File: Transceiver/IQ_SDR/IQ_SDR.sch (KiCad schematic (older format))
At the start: 198 parts, among them CON1 SJ1-3523N, J1 ANT, J10 LO_I, J11 LO_Q, J12 GNDA, J13 I_IN, J14 Q_IN, J15 +5V, J16 4.3V, J17 I_OUT, J18 Q_OUT, J19 Conn_01x01_Male, J2 GND, J20 Conn_01x01_Male, J21 V_CC, J22 Ba, J23 Bb, J24 Cb, J25 Ca, J26 Gb, J27 Ga, J28 Conn_01x02_Female, J29 Conn_01x02_Female, J3 V_IN pin header, J30 Conn_01x02_Female, J31 Conn_01x02_Female, J32 Conn_01x02_Female, J33 Conn_01x02_Female, J34 Conn_01x04_Male, J4 GND, J5 V_IN, J6 FIL_O, J7 CLK1, J8 CLK2, J9 CLK0, P1 BNC, P2 SMA, P3 SMA, P4 SMA, Q1 MMBT2222A-TP, Q10 MMBT2222A-TP, Q11 MMBT2222A-TP, Q2 2N3904, Q3 2N3904, Q4 2N3904, Q5 2N3904, Q6 MMBT2222A-TP, Q7 MMBT2222A-TP, Q8 IRF510PBF, Q9 IRF510PBF, T1 Transformer_1P_SS, T2 Transformer_1P_1S, T3 Transformer_1P_1S, T4 Transformer_SP_1S, T5 BN43-6802, U1 FST3253 or TS3A5017, U2 Si5351A-B-GT, U3 TS5A23157, U4 LM4562 or LT6231, U5 74ALVC74D, U6 Blue Pill, Y1 CX3225

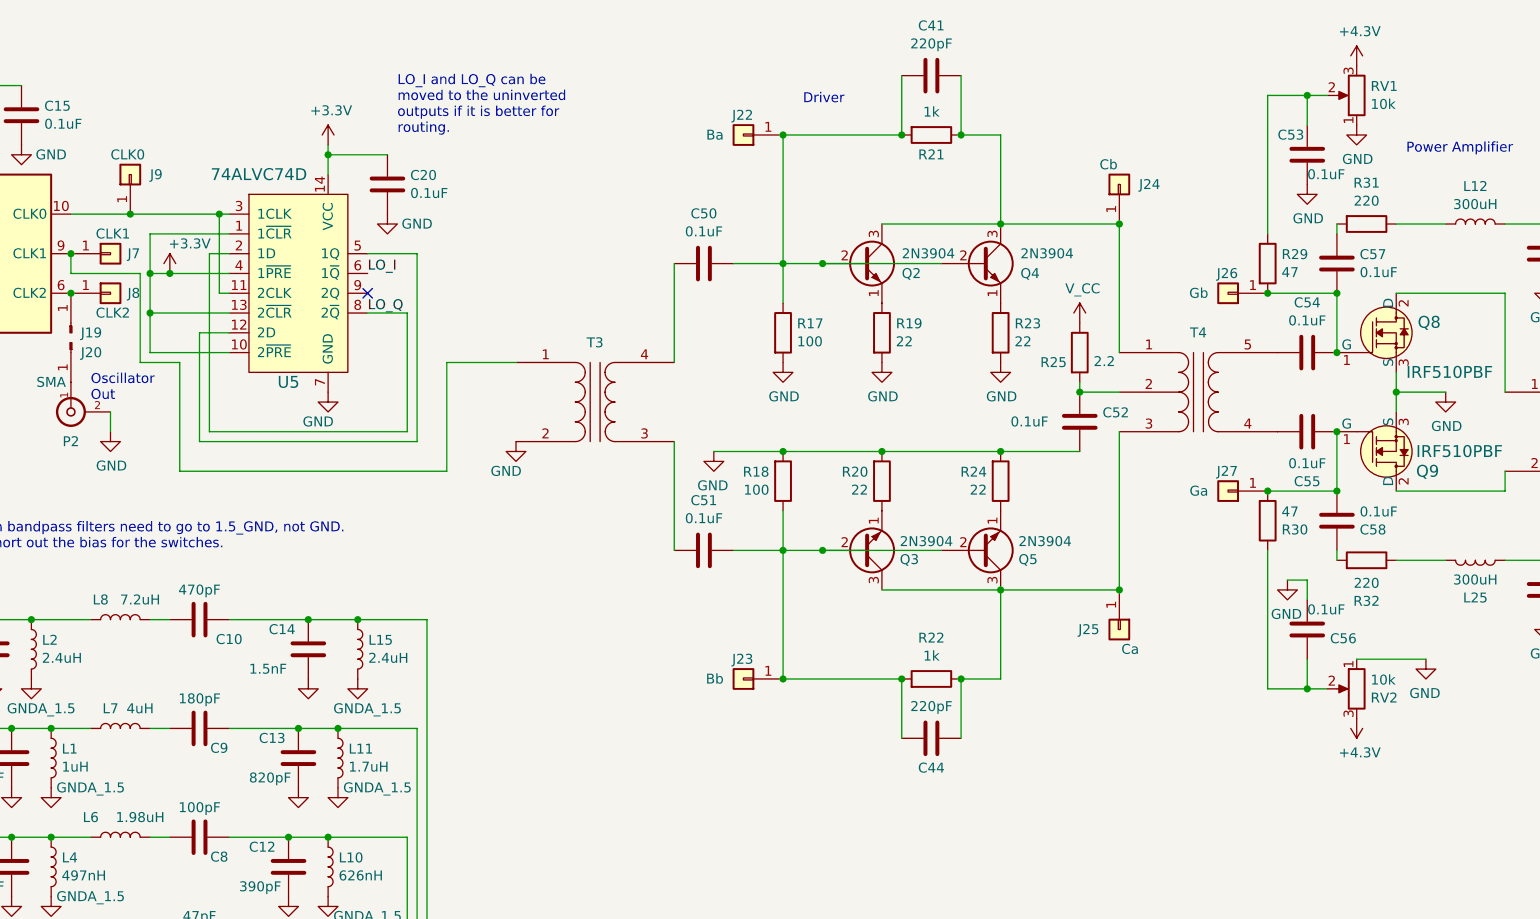
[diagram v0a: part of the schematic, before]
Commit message: Further change to schematic and moving simulations
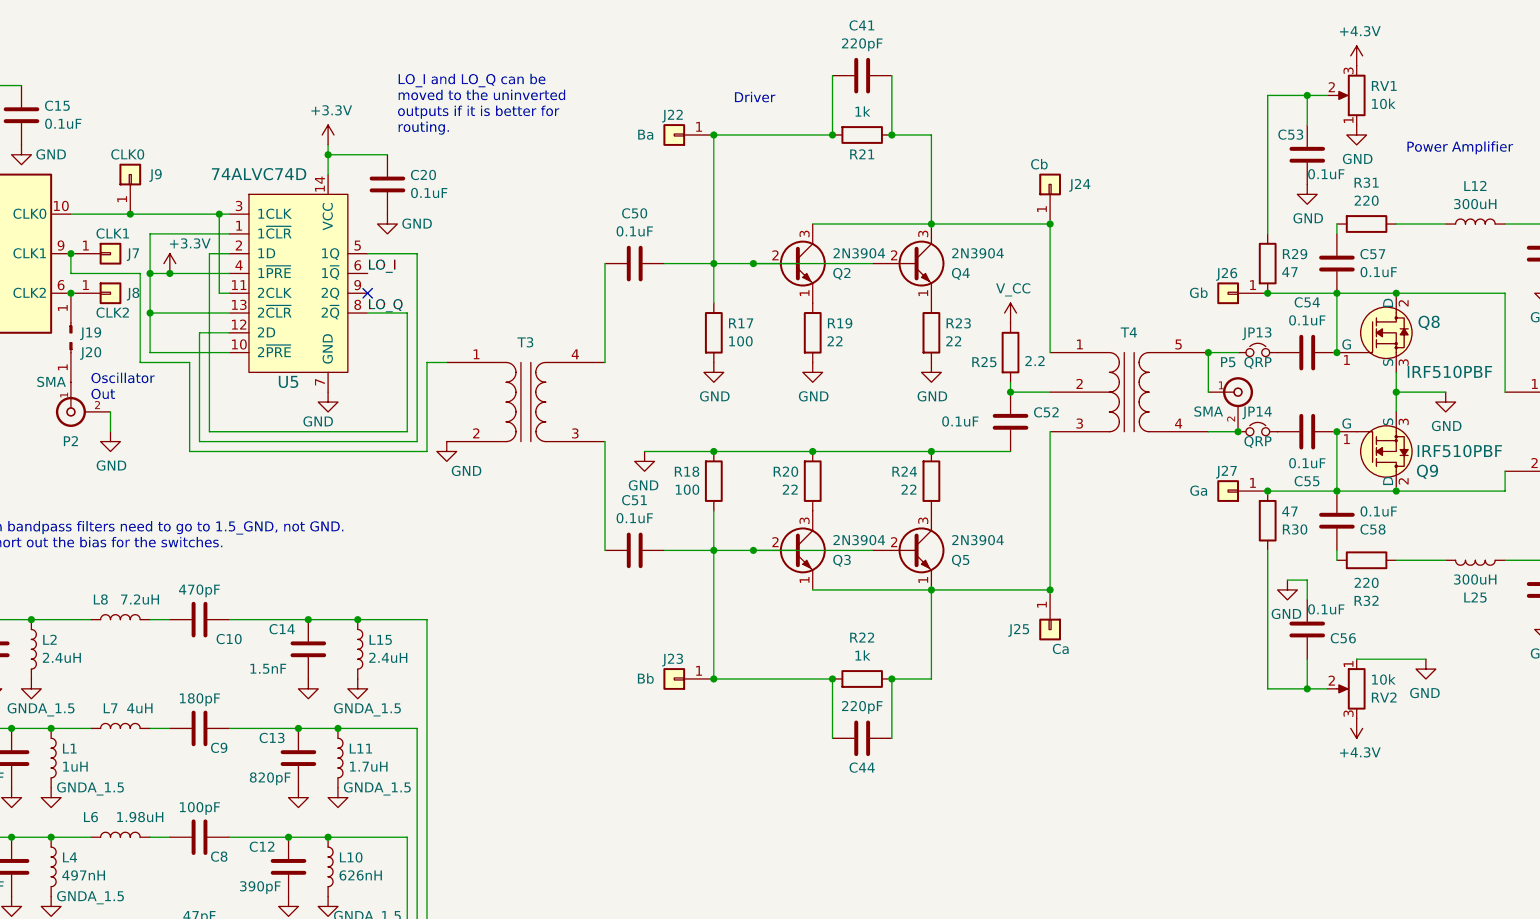
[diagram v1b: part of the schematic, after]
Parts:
- added JP13, JP14: QRP, Pin_Headers:Pin_Header_Straight_1x02_Pitch2.54mm, symbol Device:Jumper_NC_Small
- added P5: SMA, SMA:SMA_EDGE, symbol IQ_SDR-rescue:BNC-lt6231
- Q2, Q3, Q4, Q5: footprint Package_TO_SOT_THT:TO-92_Inline -> digikey-footprints:TO-92-3
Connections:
- net at C54.1, C57.1, J26.1 (Pin_1)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: now also Q8.2 (D), T5.1 (AA)
- net at C54.2: now also JP13.2; no longer T4.5 (S2)
- net at C55.1, C58.1, J27.1 (Pin_1)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: now also Q9.2 (D), T5.2 (AB)
- net at T4.4 (S1): now also JP14.1, P5.2 (Ext); no longer C55.2
- net at Q3.1 (E): now also C44.1, J25.1 (Pin_1), Q5.1 (E), R22.1, T4.3 (PR2); no longer R20.1
- net at R24.1: now also Q5.3 (C); no longer Q5.1 (E)
- new net: JP13.1, P5.1 (In), T4.5 (S2)
- new net: C55.2, JP14.2
- new net: Q3.3 (C), R20.1
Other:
- moved on the sheet: C41, C44, C50, C51, C52, J22, J23, J24, J25, Q2, R17, R18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

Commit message: PCB initial design
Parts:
- J34: footprint Pin_Headers:Pin_Header_Angled_1x04_Pitch2.54mm -> Pin_Headers:Pin_Header_Straight_1x04_Pitch2.54mm
- JP4: footprint Pin_Headers:Pin_Header_Straight_1x02_Pitch2.00mm_SMD_Pin1Right -> Pin_Headers:Pin_Header_Straight_1x02_Pitch2.54mm
- R26, R27: footprint Resistors_SMD:R_0805 -> Socket_Strips:Socket_Strip_Straight_1x02_Pitch2.54mm
- T1, T4: footprint IQ_SDR:Transformer_Toroid_Tapped_Secondary_Horizontal_D14.0mm_Amidon-T50 -> IQ_SDR:T50-2_vertical_5_pin
- T2, T3: footprint IQ_SDR:Transformer_Toroid_Tapped_Secondary_Horizontal_D14.0mm_Amidon-T50 -> IQ_SDR:T50-2_vertical_4_pin
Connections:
- net ANT_RLY: now also A1.26 (A7)
- net GND: now also T3.1 (AA); no longer T3.2 (AB)
- net SCL: now also R16.1, U6.PB6; no longer R15.1
- net SDA: now also R15.1, U6.PB7; no longer R16.1
- net TX_BAND: now also A1.25 (A6)
- net at J7.1 (Pin_1), U2.9 (CLK1): now also T3.2 (AB); no longer T3.1 (AA)
- net RFm: now reaches P1.1 (In), RLY2.9 (COM2)
- net RFb: now reaches P1.2 (Ext), RLY2.4 (COM1)
- net at C54.1, C57.1, J26.1 (Pin_1)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: no longer Q8.2 (D), T5.1 (AA)
- net PA_V_CCb: now reaches L12.1, R31.1
- net PA_V_CCb: now also Q8.2 (D), T5.1 (AA)
- net RFh: now reaches C46.1, JP12.2, L21.2, RLY1.10 (NC2)
- net RFg: now reaches C38.1, JP12.1, L17.1, RLY1.3 (NC1)
- net RFd: now reaches C47.1, L22.2, RLY1.4 (COM1)
- net RFc: now reaches C35.2, RLY1.9 (COM2)
- net at JP13.1, P5.1 (In): now also T4.4 (S1); no longer T4.5 (S2)
- net at JP14.1, P5.2 (Ext): now also T4.5 (S2); no longer T4.4 (S1)
- net at C55.1, C58.1, J27.1 (Pin_1)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: no longer Q9.2 (D), T5.2 (AB)
- net PA_V_CCc: now reaches L25.1, R32.1
- net PA_V_CCc: now also Q9.2 (D), T5.2 (AB)
- net Rfe: now reaches C34.1, JP11.1, L14.1, P4.1 (In)
- net RFf: now reaches C39.1, L14.2, L18.1
- net RFj: now reaches C43.1, L18.2, L22.1
- net RFk: now reaches C42.1, L17.2, L21.1
- net RFa: now reaches P4.2 (Ext), RLY2.5 (NO1), T5.3 (SA)
- net at C41.1, J24.1 (Pin_1), Q2.3 (C)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: now also T4.3 (PR2); no longer T4.1 (PR1)
- net at C50.2: now also T3.3 (SA); no longer T3.4 (SB)
- net at C44.1, J25.1 (Pin_1), R22.1: now also Q3.3 (C), Q5.3 (C), T4.1 (PR1); no longer Q3.1 (E), Q5.1 (E), T4.3 (PR2)
- net at R24.1: now also Q5.1 (E); no longer Q5.3 (C)
- net at R20.1: now also Q3.1 (E); no longer Q3.3 (C)
- net at C51.2: now also T3.4 (SB); no longer T3.3 (SA)
- no-connect marks 51 -> 45
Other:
- moved on the sheet: P1, R15, R16

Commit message: Commit so I can change branches.
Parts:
- U1: value FST3253 or TS3A5017 -> FST3253
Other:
- note added: "Doubly Balanced\nMixers"
- note removed: "Doubly Balanced\nSampling Mixers"
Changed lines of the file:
@@
 	1450 7200 1550 7200
 Text Notes 6050 8050 0    50   ~ 0
-Doubly Balanced\nSampling Mixers
+Doubly Balanced\nMixers
 $Comp
 L onsemi:FST3253 U1
@@
 P 3000 6750
 F 0 "U1" V 3046 5920 50  0000 R CNN
-F 1 "FST3253 or TS3A5017 " V 2950 6300 50  0000 R CNN
+F 1 "FST3253" V 2950 6300 50  0000 R CNN
 F 2 "Housings_SSOP:TSSOP-16_4.4x5mm_Pitch0.65mm" H 3000 5850 50  0001 C CNN
 F 3 "https://www.onsemi.com/pub/Collateral/FST3253-D.pdf" H 3000 5650 50  0001 C CNN

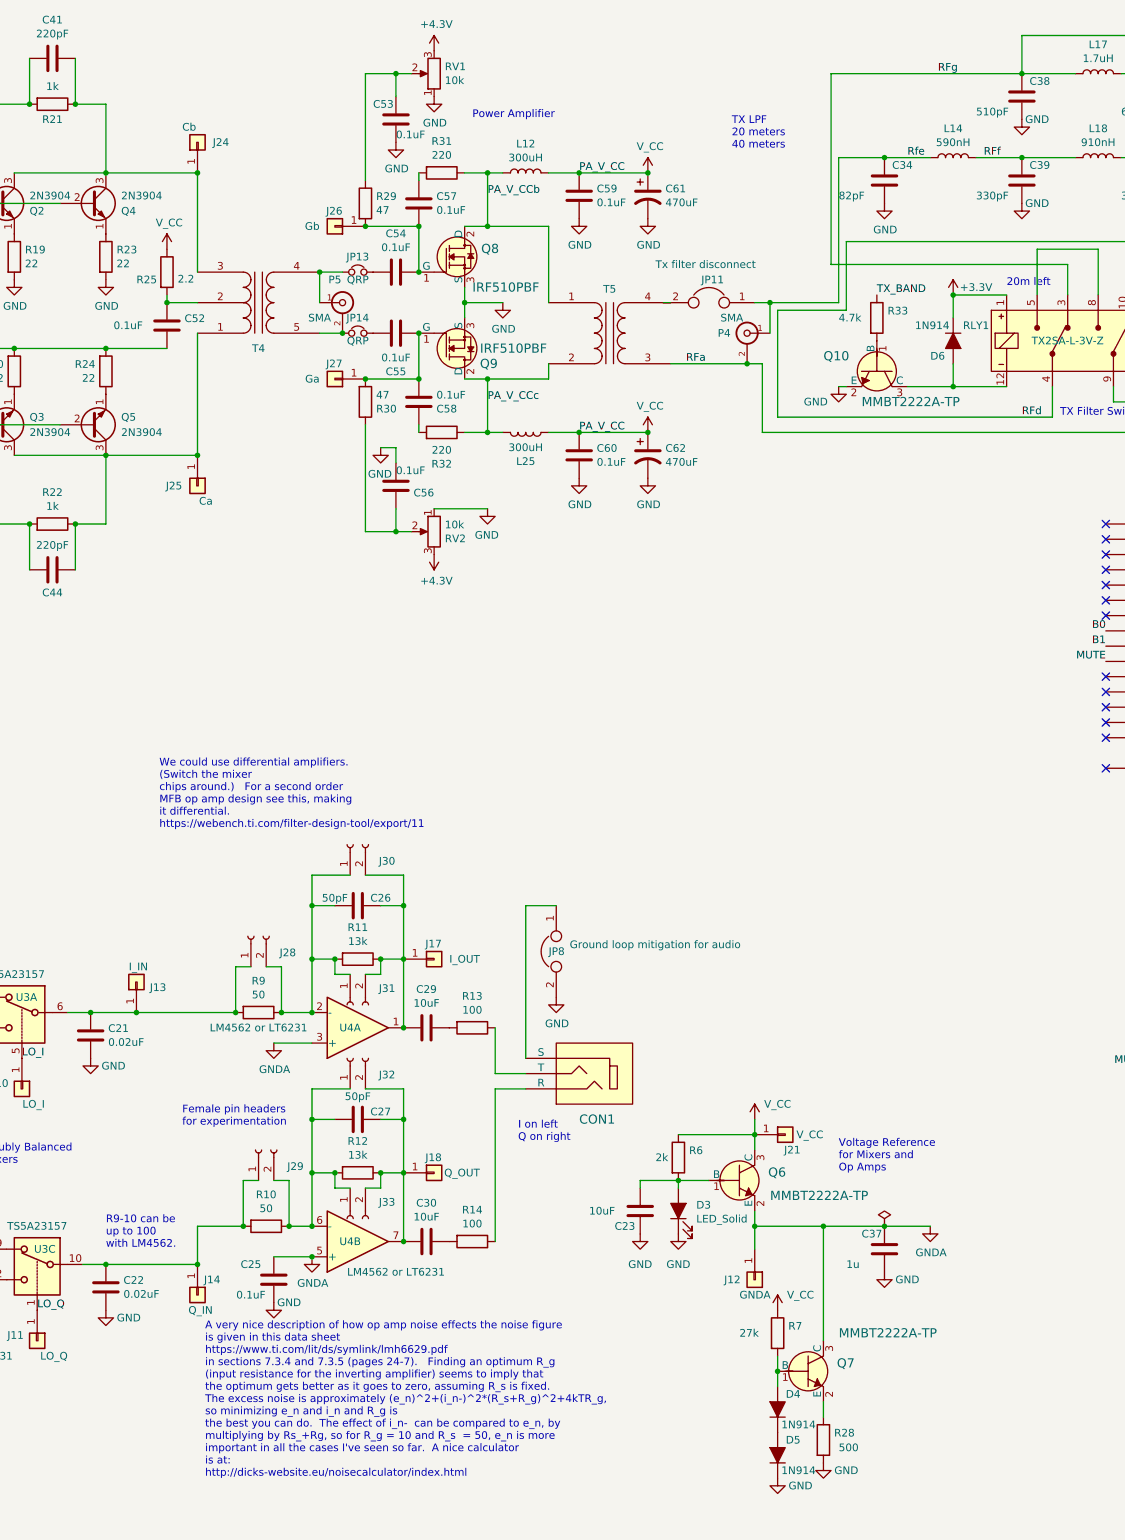
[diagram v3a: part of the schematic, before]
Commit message: Changes after build, mostly with wrong footprints for parts on hand.
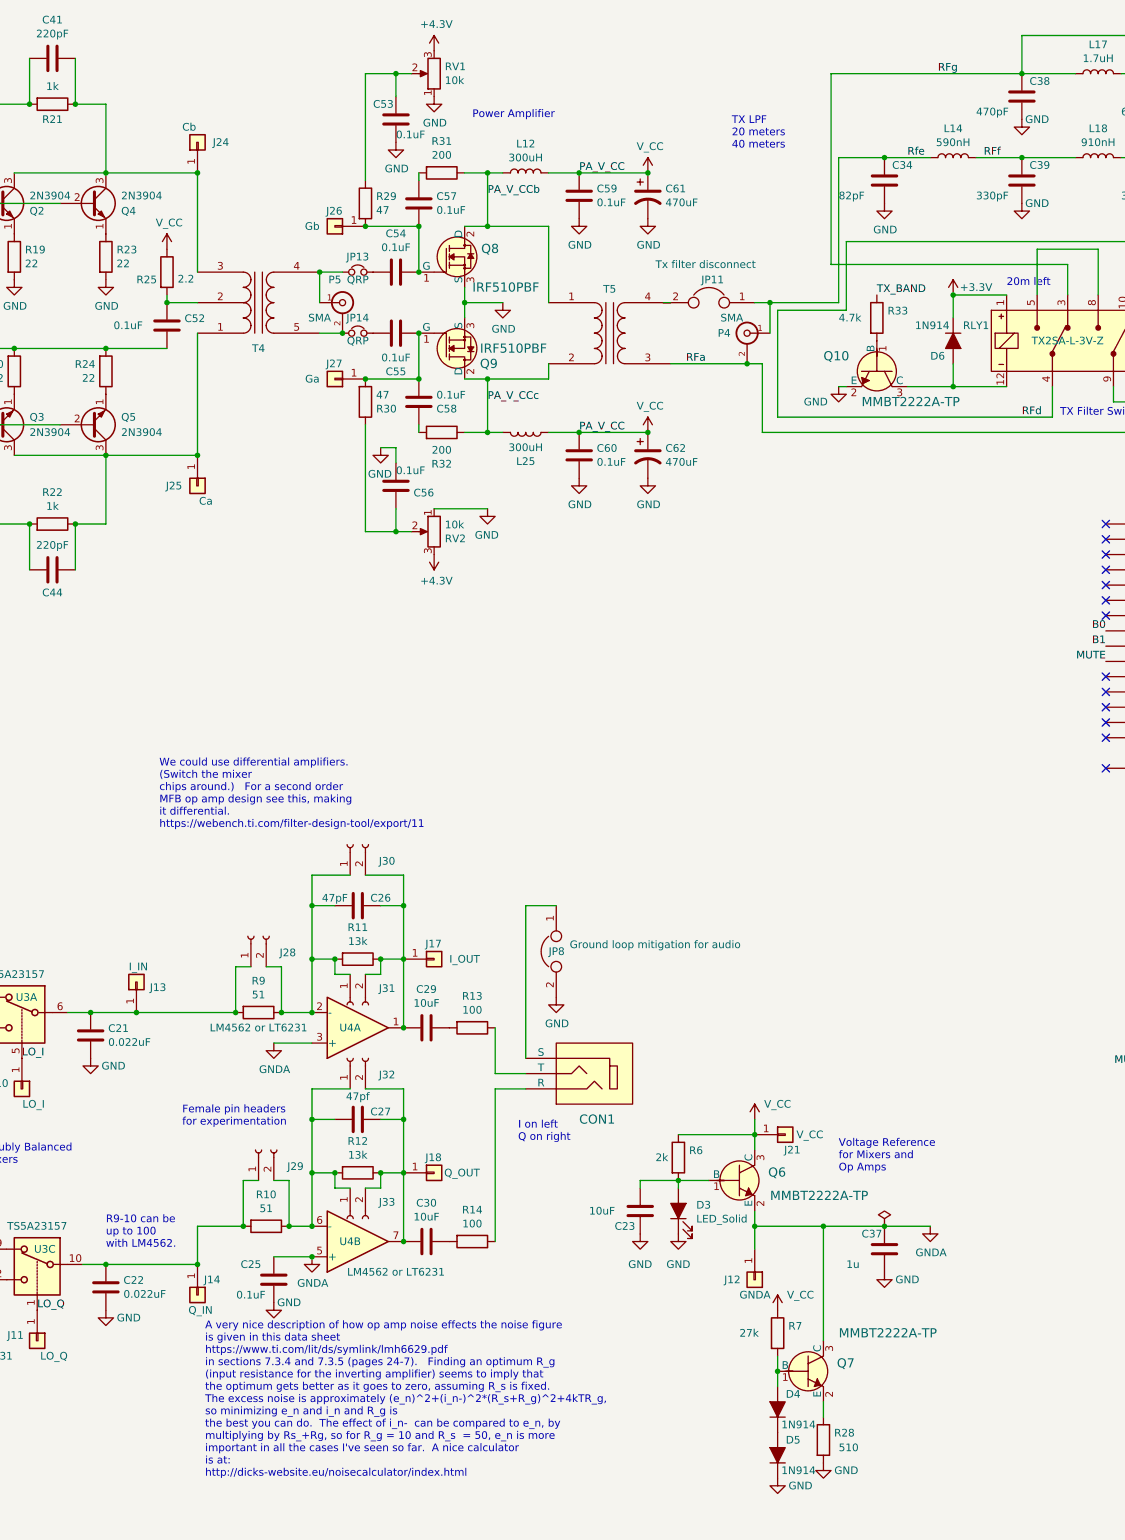
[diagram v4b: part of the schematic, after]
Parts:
- C21, C22: value 0.02uF -> 0.022uF
- C26: value 50pF -> 47pF
- C27: value 50pF -> 47pf
- C38: value 510pF -> 470pF
- R10, R9: value 50 -> 51
- R28: value 500 -> 510
- R31, R32: value 220 -> 200
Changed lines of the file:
@@
 P 6850 8850
 F 0 "C22" H 6965 8896 50  0000 L CNN
-F 1 "0.02uF" H 6965 8805 50  0000 L CNN
+F 1 "0.022uF" H 6965 8805 50  0000 L CNN
 F 2 "Capacitors_SMD:C_0805" H 6888 8700 50  0001 C CNN
 F 3 "~" H 6850 8850 50  0001 C CNN
@@
 P 6750 7200
 F 0 "C21" H 6865 7246 50  0000 L CNN
-F 1 "0.02uF" H 6865 7155 50  0000 L CNN
+F 1 "0.022uF" H 6865 7155 50  0000 L CNN
 F 2 "Capacitors_SMD:C_0805" H 6788 7050 50  0001 C CNN
 F 3 "~" H 6750 7200 50  0001 C CNN
@@
 P 7900 8450
 F 0 "R10" V 7693 8450 50  0000 C CNN
-F 1 "50" V 7784 8450 50  0000 C CNN
+F 1 "51" V 7784 8450 50  0000 C CNN
 F 2 "Resistors_SMD:R_0805" V 7830 8450 50  0001 C CNN
 F 3 "~" H 7900 8450 50  0001 C CNN
@@
 P 8500 7750
 F 0 "C27" V 8450 7900 50  0000 C CNN
-F 1 "50pF" V 8350 7750 50  0000 C CNN
+F 1 "47pf" V 8350 7750 50  0000 C CNN
 F 2 "Capacitors_SMD:C_0805" H 8538 7600 50  0001 C CNN
 F 3 "~" H 8500 7750 50  0001 C CNN
@@
 P 7850 7050
 F 0 "R9" V 7643 7050 50  0000 C CNN
-F 1 "50" V 7734 7050 50  0000 C CNN
+F 1 "51" V 7734 7050 50  0000 C CNN
 F 2 "Resistors_SMD:R_0805" V 7780 7050 50  0001 C CNN
 F 3 "~" H 7850 7050 50  0001 C CNN
@@
 P 8500 6350
 F 0 "C26" V 8450 6500 50  0000 C CNN
-F 1 "50pF" V 8450 6200 50  0000 C CNN
+F 1 "47pF" V 8450 6200 50  0000 C CNN
 F 2 "Capacitors_SMD:C_0805" H 8538 6200 50  0001 C CNN
 F 3 "~" H 8500 6350 50  0001 C CNN
@@
 P 12850 1050
 F 0 "C38" H 12900 1150 50  0000 L CNN
-F 1 "510pF" H 12550 950 50  0000 L CNN
+F 1 "470pF" H 12550 950 50  0000 L CNN
 F 2 "Capacitors_SMD:C_0805" H 12888 900 50  0001 C CNN
 F 3 "~" H 12850 1050 50  0001 C CNN
@@
 P 11550 9850
 F 0 "R28" H 11620 9896 50  0000 L CNN
-F 1 "500" H 11650 9800 50  0000 L CNN
+F 1 "510" H 11650 9800 50  0000 L CNN
 F 2 "Resistors_SMD:R_0805" V 11480 9850 50  0001 C CNN
 F 3 "~" H 11550 9850 50  0001 C CNN
@@
 P 9050 1550
 F 0 "R31" V 8843 1550 50  0000 C CNN
-F 1 "220" V 8934 1550 50  0000 C CNN
+F 1 "200" V 8934 1550 50  0000 C CNN
 F 2 "Resistors_SMD:R_0805" V 8980 1550 50  0001 C CNN
 F 3 "~" H 9050 1550 50  0001 C CNN
@@
 P 9050 3250
 F 0 "R32" V 8843 3250 50  0000 C CNN
-F 1 "220" V 8934 3250 50  0000 C CNN
+F 1 "200" V 8934 3250 50  0000 C CNN
 F 2 "Resistors_SMD:R_0805" V 8980 3250 50  0001 C CNN
 F 3 "~" H 9050 3250 50  0001 C CNN

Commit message: schematic changes
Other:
- note added: "Don't USE!"
- note added: "Don't use +5V. \nYou need +3.3V \nto program over \nserial."
- note removed: "+5V"
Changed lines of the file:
@@
 RX
 Text Notes 15500 5350 0    50   ~ 0
-+5V
+Don't USE!
 Text Notes 15500 5450 0    50   ~ 0
 DGND
@@
 Text Label 15200 2850 0    50   ~ 0
 RFn
+Text Notes 15700 5200 0    50   ~ 0
+Don't use +5V.  \nYou need +3.3V \nto program over \nserial.
 $EndSCHEMATC
